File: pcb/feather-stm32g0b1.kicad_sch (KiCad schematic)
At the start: 15 parts, among them SW1 SW_Push, U1 STM32G0B1CBT6, Y1 32.768 KHz, 10ppm, 12.5pf, Y2 8 MHz, 10ppm, 10pf

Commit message: Lots more work on RevB schematics and pcb
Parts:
- added R16, R17: 5K1, Resistor_SMD:R_0402_1005Metric, symbol Device:R
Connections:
- net +3V3: now also R16.1, R17.1
- net ANALOG0: now also U1.15 (PA4); no longer U1.11 (PA0)
- net ANALOG1: now also U1.16 (PA5); no longer U1.12 (PA1)
- net ANALOG4: now also U1.11 (PA0); no longer U1.15 (PA4)
- net ANALOG5: now also U1.12 (PA1); no longer U1.16 (PA5)
- net DIGITAL10: now also U1.45 (PB6); no longer U1.38 (PD0)
- net DIGITAL11: now also U1.46 (PB7); no longer U1.39 (PD1)
- net DIGITAL12: now also U1.47 (PB8); no longer U1.40 (PD2)
- net DIGITAL13: now also U1.48 (PB9); no longer U1.41 (PD3)
- net DIGITAL5: now also U1.19 (PB0); no longer U1.27 (PB15)
- net DIGITAL6: now also U1.17 (PA6); no longer U1.28 (PA8)
- net DIGITAL9: now also U1.44 (PB5); no longer U1.37 (PA15)
- net I2C3_SCL: now also R17.2
- net I2C3_SDA: now also R16.2

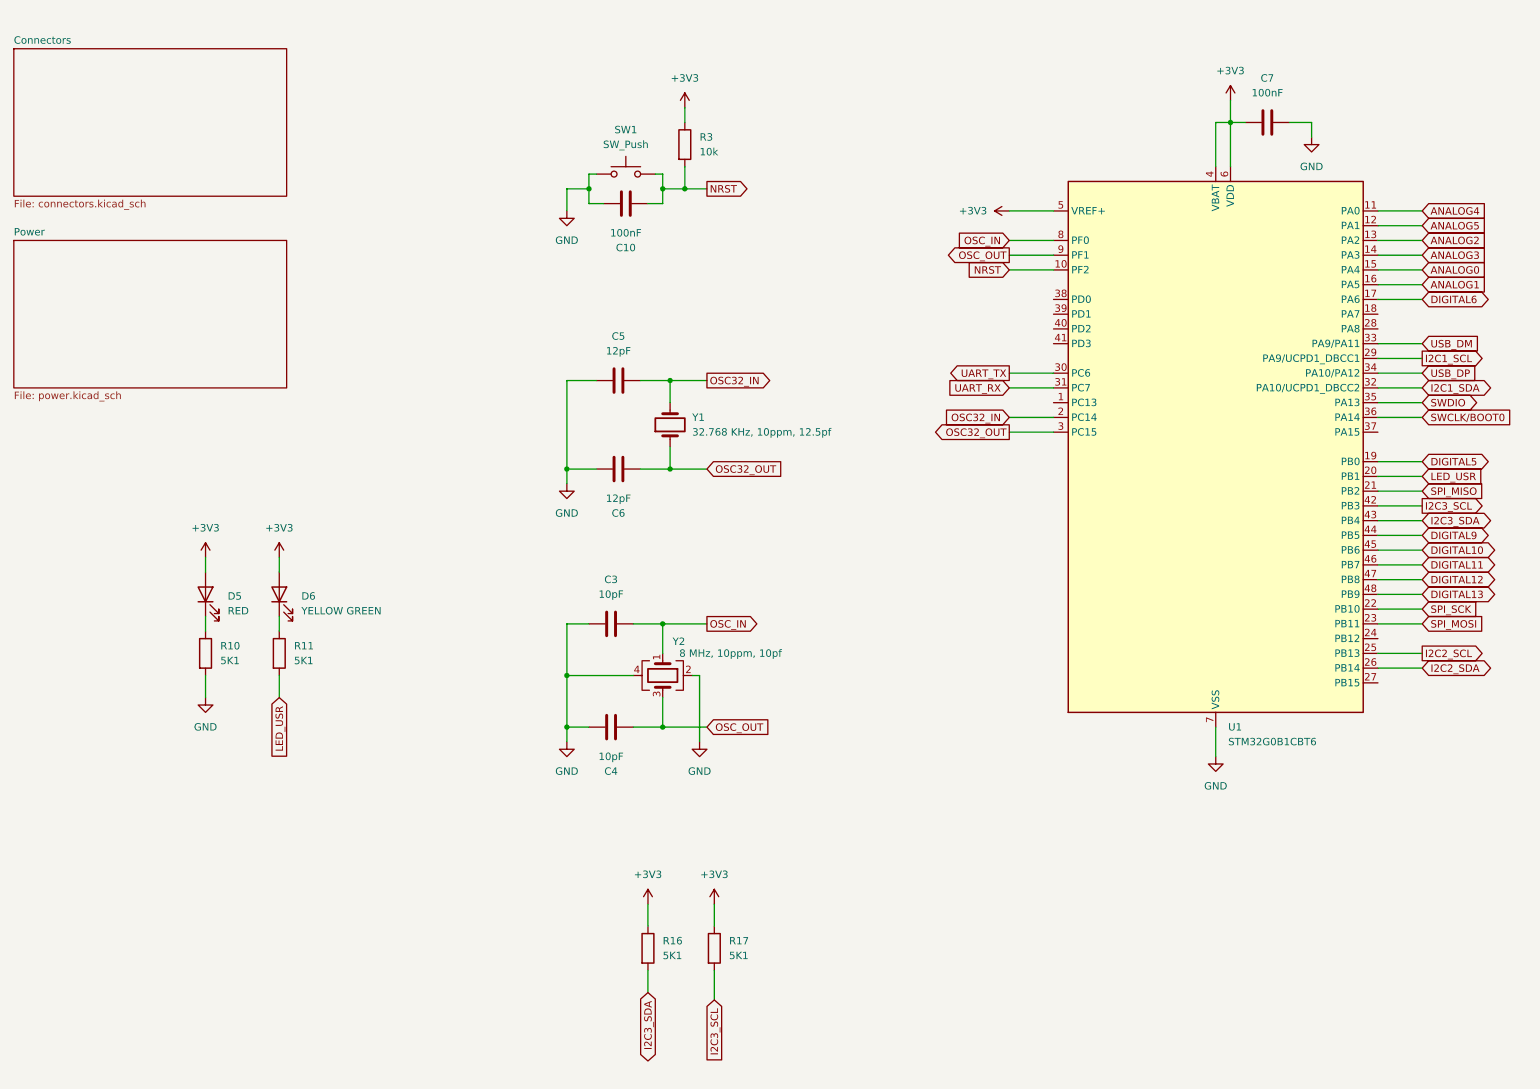
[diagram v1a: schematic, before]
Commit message: Added I2C pull ups, extra bypass capacitance for the MCU and increased the LDO output capacitance
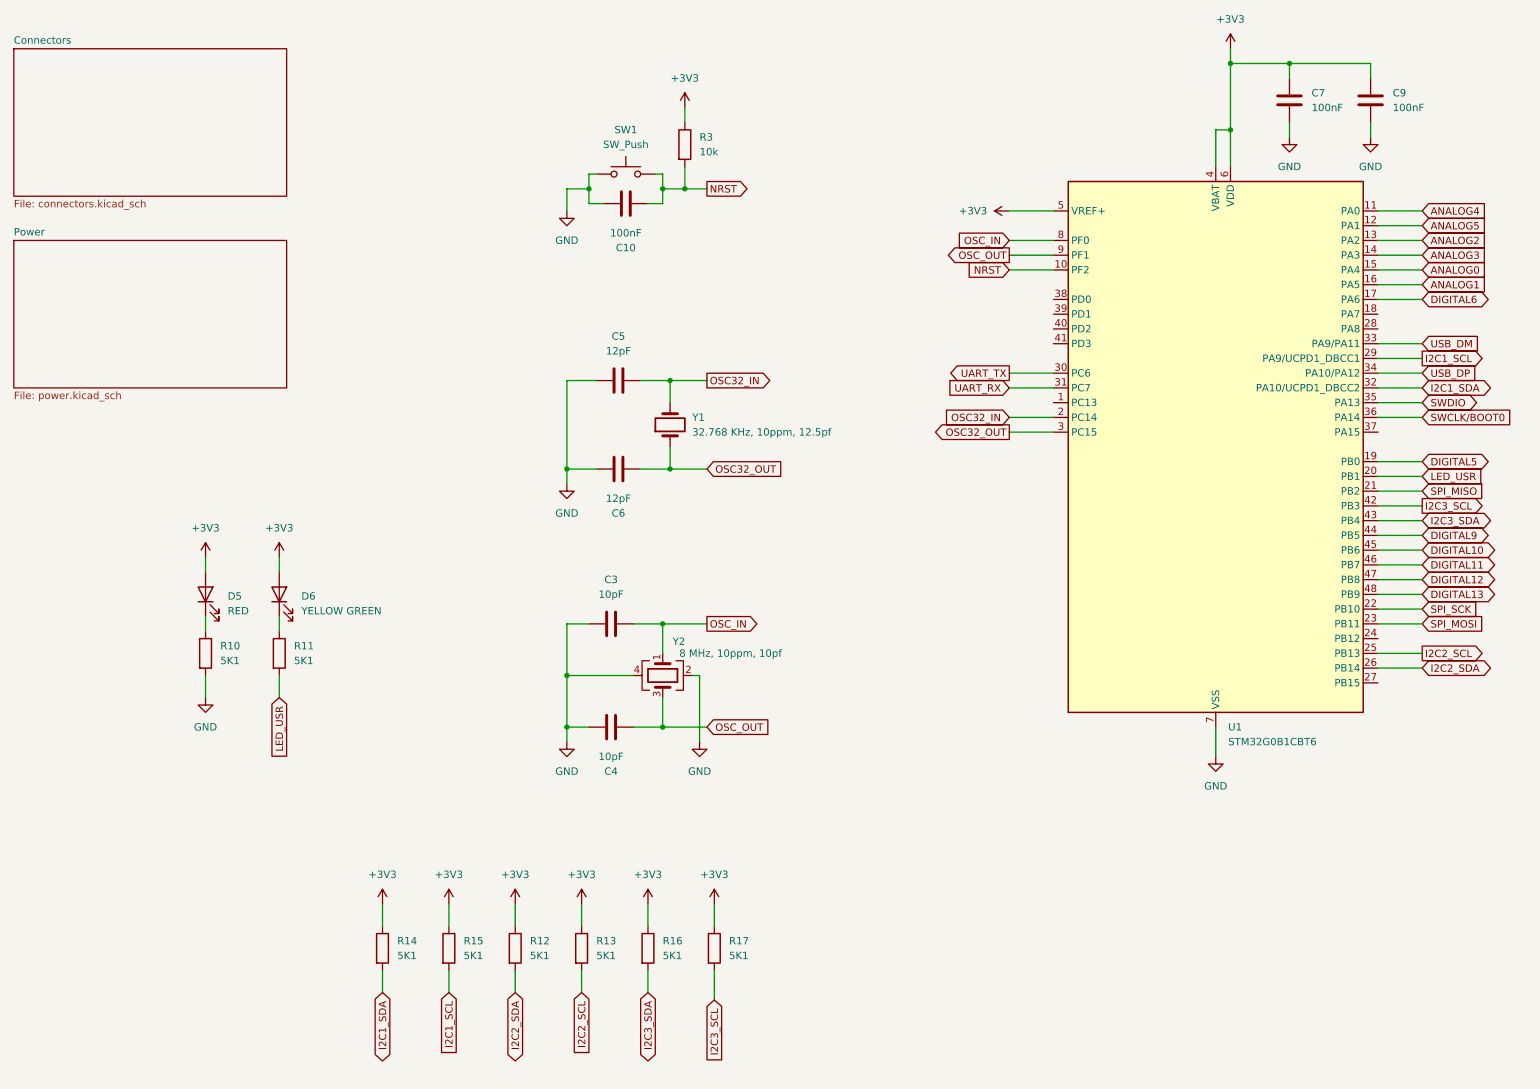
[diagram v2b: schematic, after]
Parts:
- added C9: 100nF, Capacitor_SMD:C_0402_1005Metric, symbol Device:C
- added R12, R13, R14, R15: 5K1, Resistor_SMD:R_0402_1005Metric, symbol Device:R
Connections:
- net +3V3: now also C7.2, C9.2, R12.1, R13.1, R14.1, R15.1; no longer C7.1
- net GND: now also C7.1, C9.1; no longer C7.2
- net I2C1_SCL: now also R15.2
- net I2C1_SDA: now also R14.2
- net I2C2_SCL: now also R13.2
- net I2C2_SDA: now also R12.2
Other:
- moved on the sheet: C7

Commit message: More PCB layout updates
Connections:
- net USB_DM renamed USB_DN
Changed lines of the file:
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@@
 		)
 	)
-	(global_label "USB_DM"
+	(global_label "USB_DN"
 		(shape input)
 		(at 260.35 69.85 0)
@@
 		)
 		(property "Intersheetrefs" "${INTERSHEET_REFS}"
-			(at 270.8342 69.85 0)
+			(at 270.7133 69.85 0)
 			(effects
 				(font

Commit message: Used kibuzzard to generate nice labels for buttons, ports and leds
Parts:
- SW1: footprint Button_Switch_SMD:SW_SPST_B3U-1000P -> prop-devboard:WUERTH_434153017835; LCSC Part # C231329 -> C2680612
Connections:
- net GND: now also SW1.2; no longer SW1.1
- net NRST: now also SW1.1; no longer SW1.2
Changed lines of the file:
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@@
 		(lib_id "Switch:SW_Push")
 		(at 123.19 40.64 0)
+		(mirror y)
 		(unit 1)
 		(body_style 1)
@@
 		(in_pos_files yes)
 		(dnp no)
-		(fields_autoplaced yes)
 		(property "Reference" "SW1"
 			(at 123.19 33.02 0)
@@
 			)
 		)
-		(property "Footprint" "Button_Switch_SMD:SW_SPST_B3U-1000P"
+		(property "Footprint" "prop-devboard:WUERTH_434153017835"
 			(at 123.19 35.56 0)
 			(hide yes)
@@
 			)
 		)
-		(property "LCSC Part #" "C231329"
+		(property "LCSC Part #" "C2680612"
 			(at 123.19 40.64 0)
 			(hide yes)

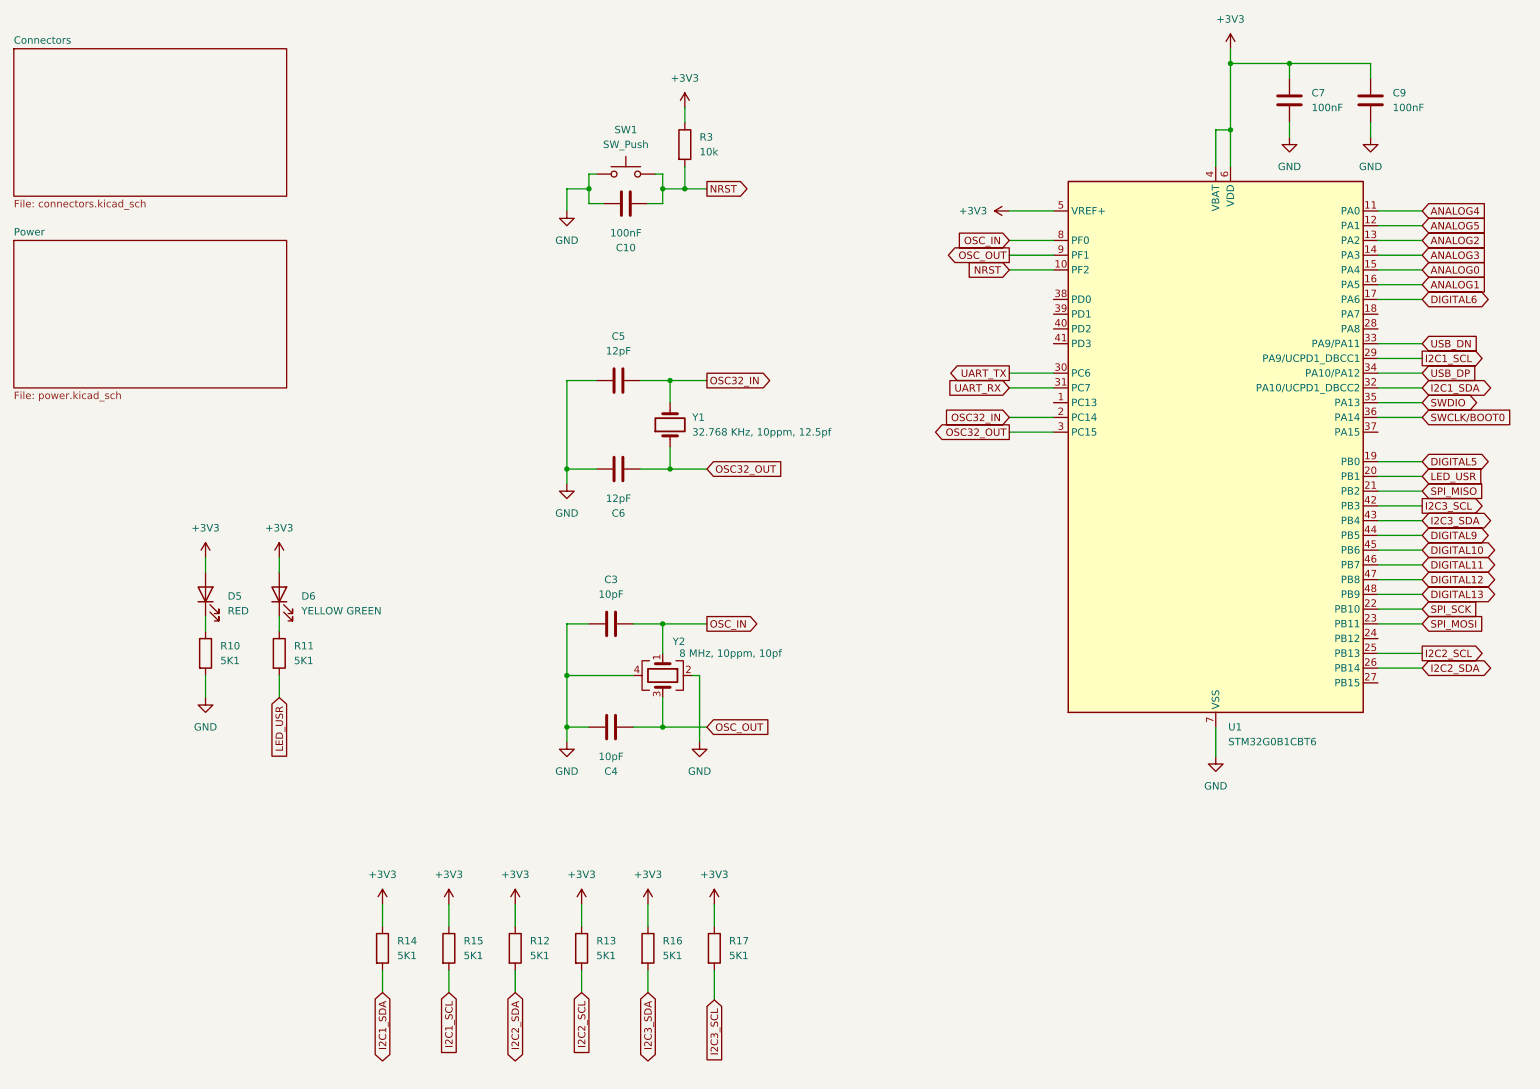
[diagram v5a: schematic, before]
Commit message: Added I2C EEPROM to the board
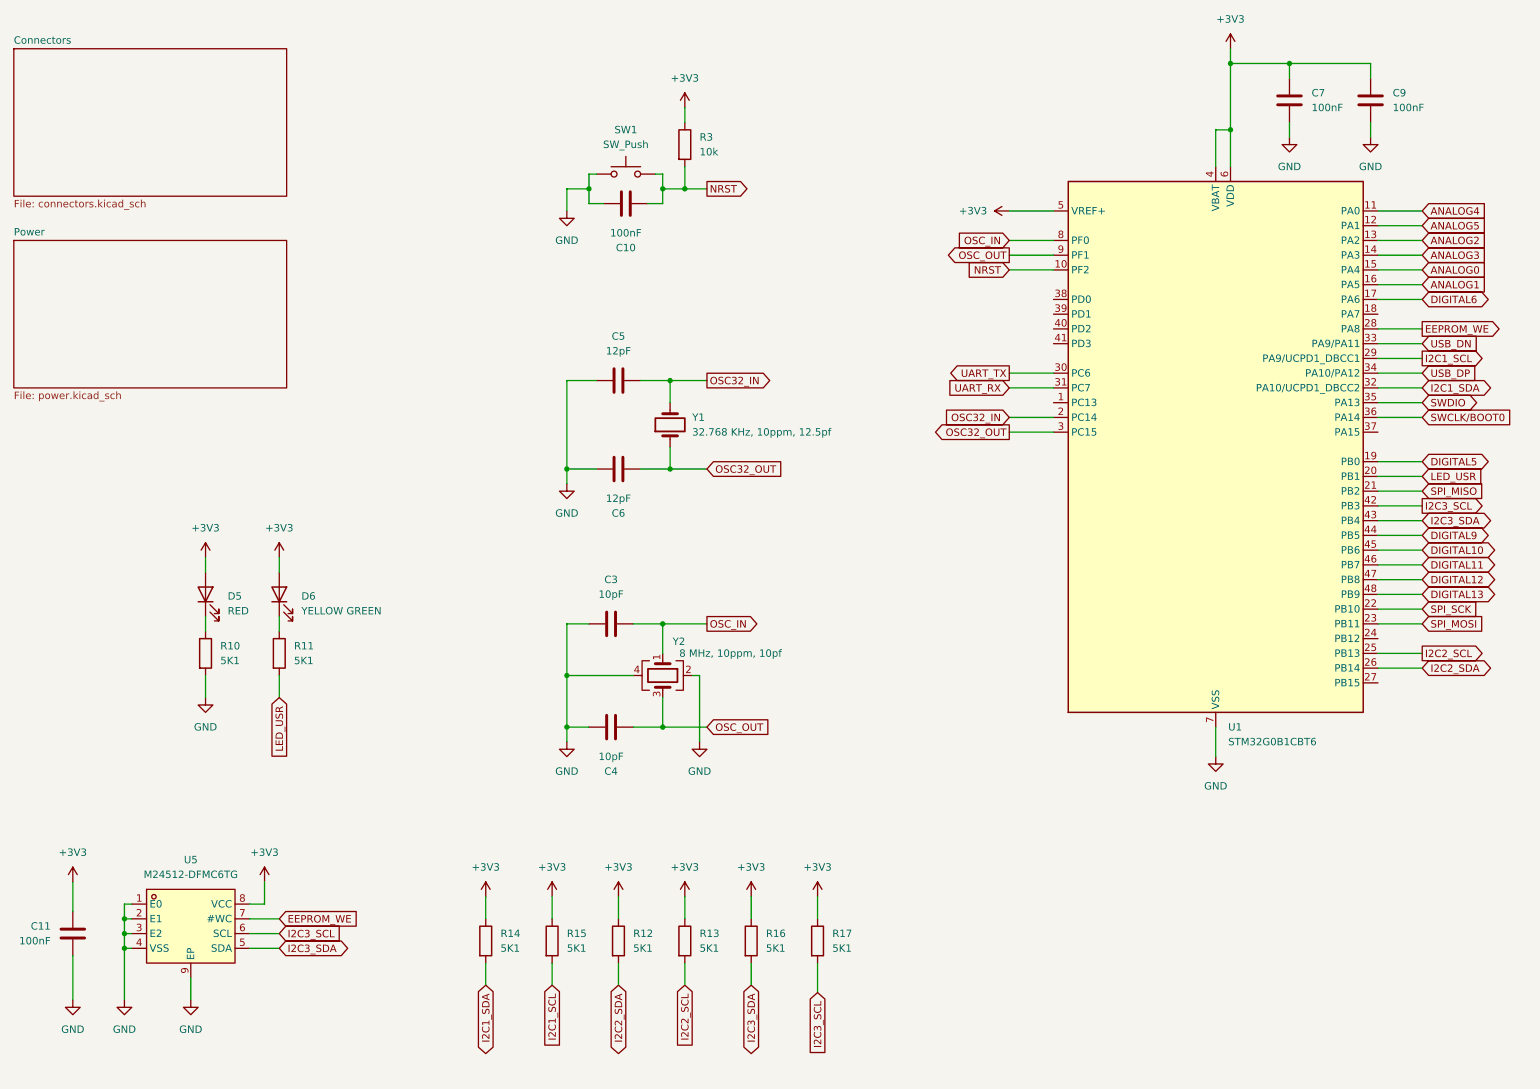
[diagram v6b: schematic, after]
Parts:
- added C11: 100nF, Capacitor_SMD:C_0402_1005Metric, symbol Device:C
- added U5: M24512-DFMC6TG, prop-devboard:DFN-8_L3.0-W2.0-P0.50-BL-EP, symbol prop-devboard:M24512-DFMC6TG
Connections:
- net +3V3: now also C11.2, U5.8 (VCC)
- net GND: now also C11.1, U5.1 (E0), U5.2 (E1), U5.3 (E2), U5.4 (VSS), U5.9 (EP)
- net I2C3_SCL: now also U5.6 (SCL)
- net I2C3_SDA: now also U5.5 (SDA)
- net EEPROM_WE: now reaches U1.28 (PA8)
- net EEPROM_WE: now also U5.7 (#WC)
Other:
- moved on the sheet: R12, R13, R14, R15, R16, R17
